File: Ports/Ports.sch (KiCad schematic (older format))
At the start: 22 parts, among them J1 Conn_01x09_Male, J2 Conn_01x09_Male, J3 Conn_01x09_Male, J4 Screw_Terminal_01x02, J5 Conn_01x03_Male, U1 74LS574, U2 74LS574

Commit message: Polishing Ports
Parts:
- C1: footprint Capacitor_THT:C_Disc_D5.1mm_W3.2mm_P5.00mm -> Capacitor_THT:C_Disc_D9.0mm_W5.0mm_P10.00mm
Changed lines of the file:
@@
 F 0 "C1" H 6615 5196 50  0000 L CNN
 F 1 "0.1uF" H 6615 5105 50  0000 L CNN
-F 2 "Capacitor_THT:C_Disc_D5.1mm_W3.2mm_P5.00mm" H 6538 5000 50  0001 C CNN
+F 2 "Capacitor_THT:C_Disc_D9.0mm_W5.0mm_P10.00mm" H 6538 5000 50  0001 C CNN
 F 3 "~" H 6500 5150 50  0001 C CNN
 	1    6500 5150

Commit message: Polishing Ports
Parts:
- removed J5: Conn_01x03_Male, Connector_PinHeader_2.54mm:PinHeader_1x03_P2.54mm_Vertical, symbol Connector:Conn_01x03_Male
- added D1, D10, D2, D3, D4, D5, D6, D7, D8, D9: LED, LED_THT:LED_Rectangular_W5.0mm_H2.0mm, symbol Device:LED
- added J5: Conn_01x04_Male, Connector_PinHeader_2.54mm:PinHeader_1x04_P2.54mm_Horizontal, symbol Connector:Conn_01x04_Male
- added R10, R11, R12, R13, R4, R5, R6, R7, R8, R9: 1k, Resistor_SMD:R_0805_2012Metric_Pad1.20x1.40mm_HandSolder, symbol Device:R
- J1: footprint Connector_PinHeader_2.54mm:PinHeader_1x09_P2.54mm_Vertical -> Connector_PinHeader_2.54mm:PinHeader_1x09_P2.54mm_Horizontal
- R1: footprint Resistor_THT:R_Axial_DIN0207_L6.3mm_D2.5mm_P10.16mm_Horizontal -> Resistor_THT:R_Axial_DIN0207_L6.3mm_D2.5mm_P15.24mm_Horizontal
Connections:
- net labels added: EN
- wire segments 47 -> 59
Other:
- moved on the sheet: R1, RV1

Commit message: Ports. Try to add buttons.
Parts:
- added D11, D12, D13, D14, D15, D16, D17, D18, D19, D20, D21, D22, D23, D24, D25, D26: 6x6-tact-btn, CommonLibrary:6x6-tact-btn, symbol CommonLibrary:6x6-tact-btn
- added D27, D28: LL4148, Diode_SMD:D_MiniMELF, symbol Diode:LL4148
- added J6: Conn_01x09_Male, Connector_PinHeader_2.54mm:PinHeader_1x09_P2.54mm_Horizontal, symbol Connector:Conn_01x09_Male
- added J7: Conn_01x02_Male, Connector_PinHeader_2.54mm:PinHeader_1x02_P2.54mm_Horizontal, symbol Connector:Conn_01x02_Male
- added R14, R15, R16, R17, R18, R19, R20, R21: 10k, Resistor_SMD:R_0805_2012Metric_Pad1.20x1.40mm_HandSolder, symbol Device:R
- added U3: 74LS574, Package_DIP:DIP-20_W7.62mm, symbol 74xx:74LS574
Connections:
- net GND: now also J6.9 (Pin_9), U3.10 (GND)
- net P0.6: now also D27.1 (K)
- net P0.7: now also D28.1 (K)
- net VCC: now also R14.2, R15.2, R16.2, R17.2, R18.2, R19.2, R20.2, R21.2, U3.20 (VCC)
- new net: D11.2, D13.2, D15.2, D17.2, D19.2, D21.2, D23.2, D25.2, D27.2 (A)
- new net: D12.2, D14.2, D16.2, D18.2, D20.2, D22.2, D24.2, D26.2, D28.2 (A)
- new net BUS0: J6.8 (Pin_8), U3.19 (Q0)
- new net BUS1: J6.7 (Pin_7), U3.18 (Q1)
- new net BUS2: J6.6 (Pin_6), U3.17 (Q2)
- new net BUS3: J6.5 (Pin_5), U3.16 (Q3)
- new net BUS4: J6.4 (Pin_4), U3.15 (Q4)
- new net BUS5: J6.3 (Pin_3), U3.14 (Q5)
- new net BUS6: J6.2 (Pin_2), U3.13 (Q6)
- new net BUS7: J6.1 (Pin_1), U3.12 (Q7)
- new net IN0.0: D11.1, D12.1, R14.1, U3.2 (D0)
- new net IN0.1: D13.1, D14.1, R15.1, U3.3 (D1)
- new net IN0.2: D15.1, D16.1, R16.1, U3.4 (D2)
- new net IN0.3: D17.1, D18.1, R17.1, U3.5 (D3)
- new net IN0.4: D19.1, D20.1, R18.1, U3.6 (D4)
- new net IN0.5: D21.1, D22.1, R19.1, U3.7 (D5)
- new net IN0.6: D23.1, D24.1, R20.1, U3.8 (D6)
- new net IN0.7: D25.1, D26.1, R21.1, U3.9 (D7)
- new net IN0.C: J7.1 (Pin_1), U3.11 (Cp)
- new net IN0.OE: J7.2 (Pin_2), U3.1 (OE)
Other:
- moved on the sheet: C1, C2, D1, D10, D2, D3, D4, D5, D6, D7, D8, D9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

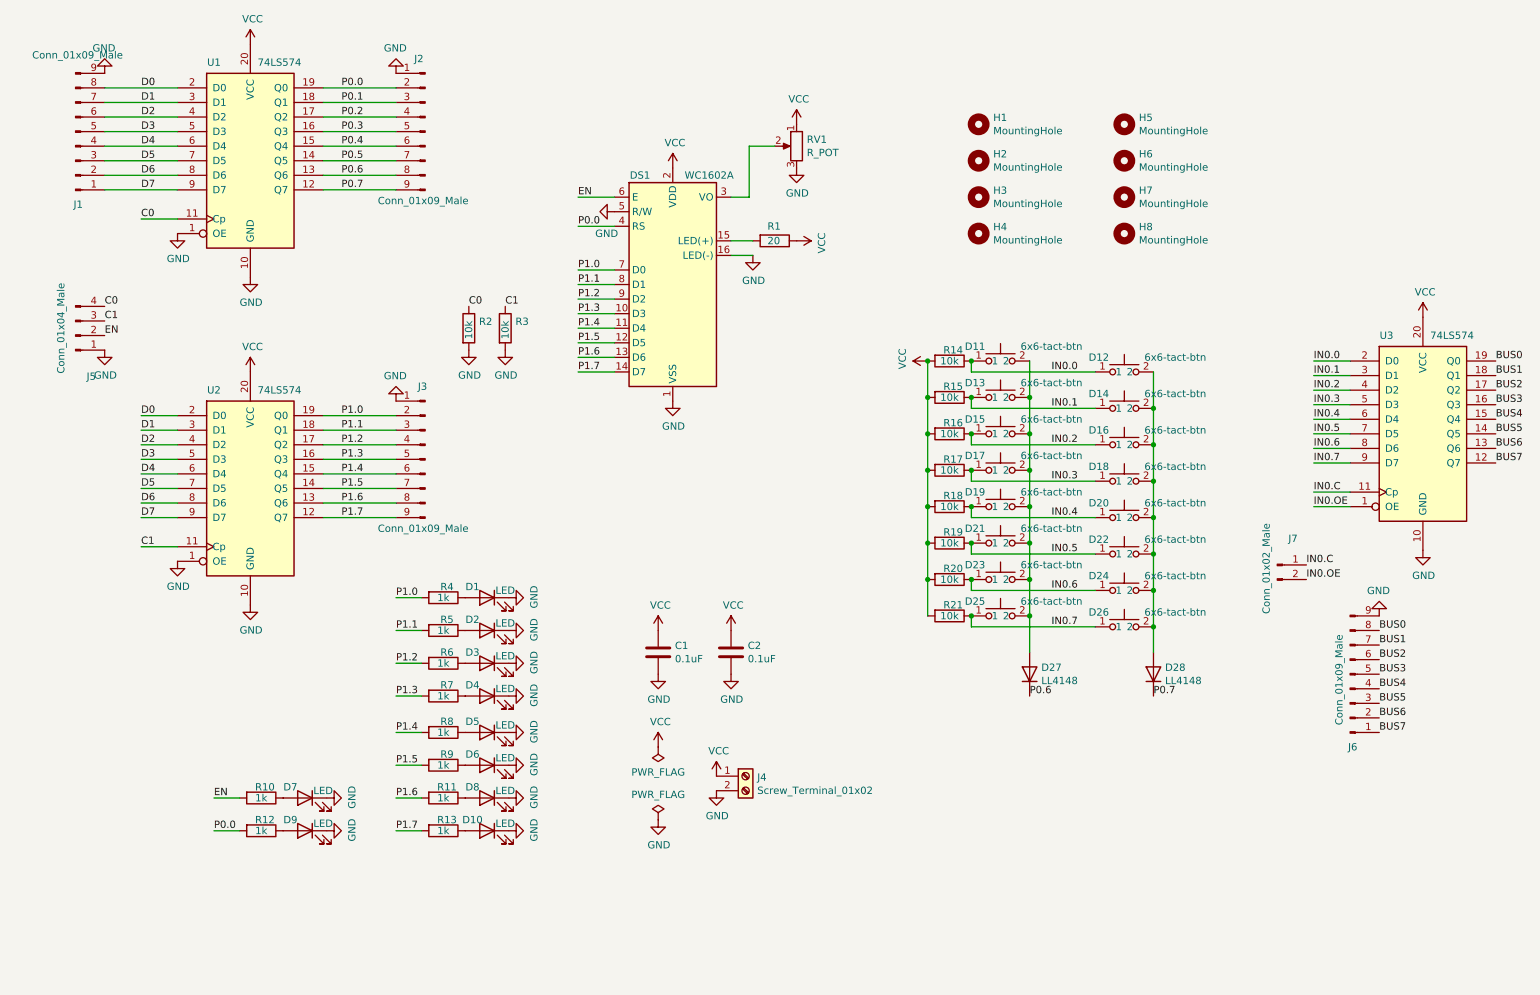
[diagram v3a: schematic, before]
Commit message: Add buttons to Ports&LCD pcb
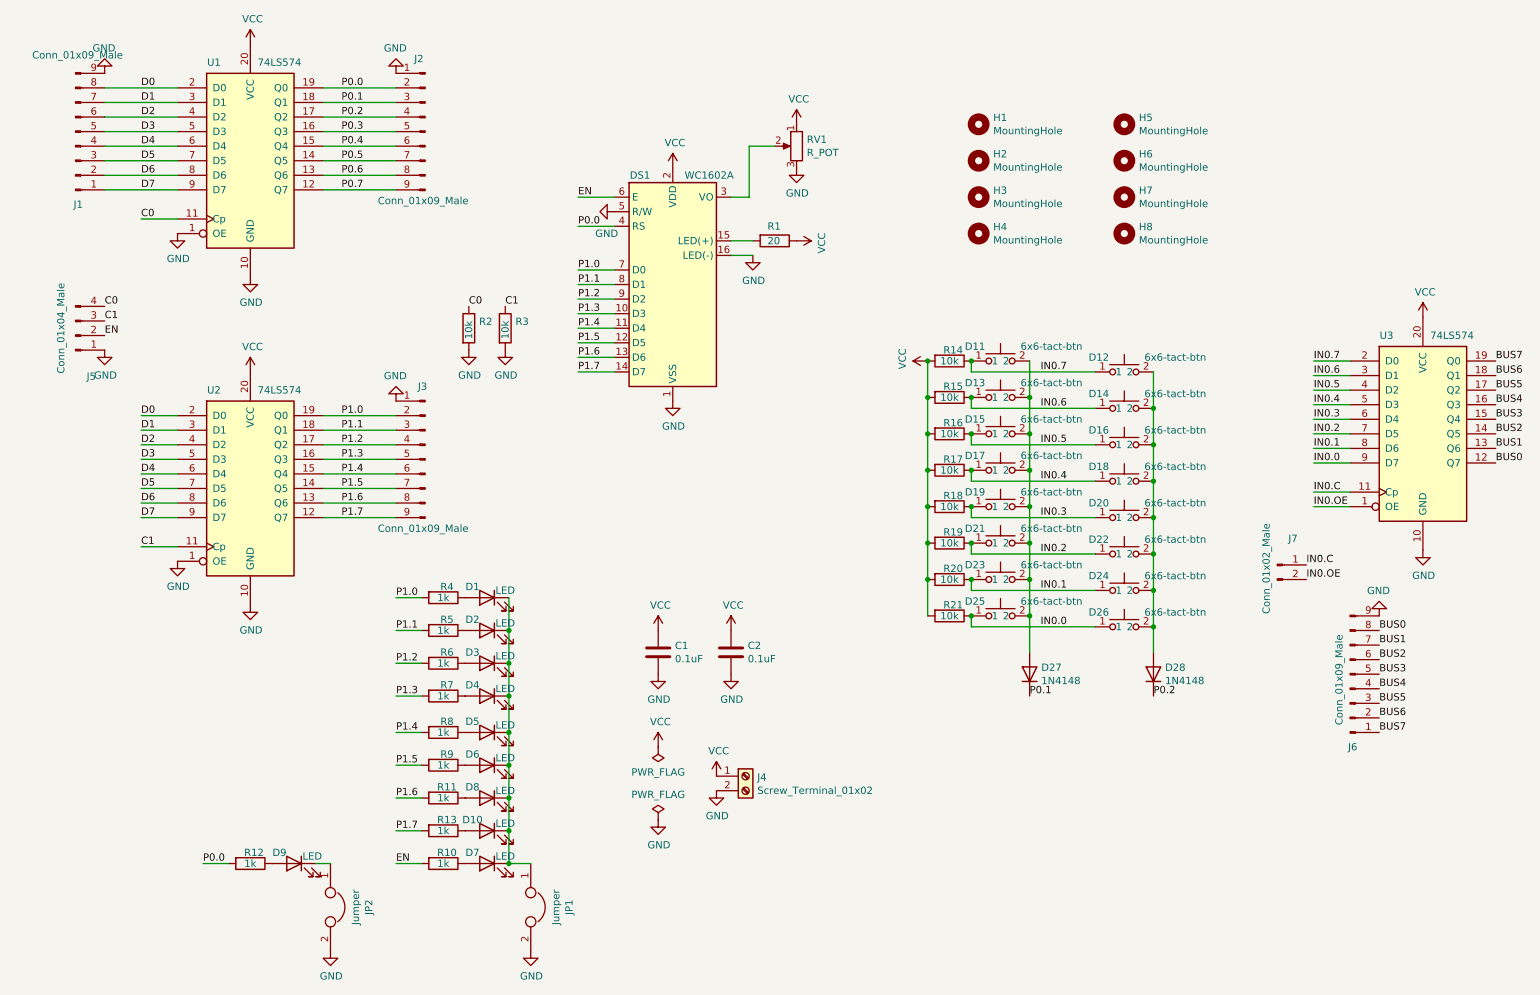
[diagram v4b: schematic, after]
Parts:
- removed D27, D28: LL4148, Diode_SMD:D_MiniMELF, symbol Diode:LL4148
- added D27, D28: 1N4148, Diode_THT:D_DO-15_P12.70mm_Horizontal, symbol Diode:1N4148
- added JP1, JP2: Jumper, Jumper:SolderJumper-2_P1.3mm_Open_RoundedPad1.0x1.5mm, symbol Device:Jumper
- D11, D12, D13, D14, D15, D16, D17, D18, D19, D20, D21, D22, D23, D24, D25, D26: footprint CommonLibrary:6x6-tact-btn -> Button_Switch_THT:SW_PUSH_6mm_H4.3mm
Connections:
- net BUS0: now also U3.12 (Q7); no longer U3.19 (Q0)
- net BUS1: now also U3.13 (Q6); no longer U3.18 (Q1)
- net BUS2: now also U3.14 (Q5); no longer U3.17 (Q2)
- net BUS3: now also U3.15 (Q4); no longer U3.16 (Q3)
- net BUS4: now also U3.16 (Q3); no longer U3.15 (Q4)
- net BUS5: now also U3.17 (Q2); no longer U3.14 (Q5)
- net BUS6: now also U3.18 (Q1); no longer U3.13 (Q6)
- net BUS7: now also U3.19 (Q0); no longer U3.12 (Q7)
- net GND: now also JP1.2, JP2.2; no longer D1.1 (K), D10.1 (K), D2.1 (K), D3.1 (K), D4.1 (K), D5.1 (K), D6.1 (K), D7.1 (K), D8.1 (K), D9.1 (K)
- net IN0.0: now also D25.1, D26.1, R21.1, U3.9 (D7); no longer D11.1, D12.1, R14.1, U3.2 (D0)
- net IN0.1: now also D23.1, D24.1, R20.1, U3.8 (D6); no longer D13.1, D14.1, R15.1, U3.3 (D1)
- net IN0.2: now also D21.1, D22.1, R19.1, U3.7 (D5); no longer D15.1, D16.1, R16.1, U3.4 (D2)
- net IN0.3: now also D19.1, D20.1, R18.1, U3.6 (D4); no longer D17.1, D18.1, R17.1, U3.5 (D3)
- net IN0.4: now also D17.1, D18.1, R17.1, U3.5 (D3); no longer D19.1, D20.1, R18.1, U3.6 (D4)
- net IN0.5: now also D15.1, D16.1, R16.1, U3.4 (D2); no longer D21.1, D22.1, R19.1, U3.7 (D5)
- net IN0.6: now also D13.1, D14.1, R15.1, U3.3 (D1); no longer D23.1, D24.1, R20.1, U3.8 (D6)
- net IN0.7: now also D11.1, D12.1, R14.1, U3.2 (D0); no longer D25.1, D26.1, R21.1, U3.9 (D7)
- net P0.1: now also D27.1 (K)
- net P0.2: now also D28.1 (K)
- net at D11.2, D13.2, D15.2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: now also D27.2 (A)
- net at D12.2, D14.2, D16.2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: now also D28.2 (A)
- new net: D1.1 (K), D10.1 (K), D2.1 (K), D3.1 (K), D4.1 (K), D5.1 (K), D6.1 (K), D7.1 (K), D8.1 (K), JP1.1
- new net: D9.1 (K), JP2.1
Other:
- moved on the sheet: D7, D9, R10, R12

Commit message: Polishing Ports & LCD
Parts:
- added C3, C4: 0.1uF, Capacitor_SMD:C_1206_3216Metric_Pad1.42x1.75mm_HandSolder, symbol Device:C
- C1: footprint Capacitor_THT:C_Disc_D9.0mm_W5.0mm_P10.00mm -> Capacitor_SMD:C_1206_3216Metric_Pad1.42x1.75mm_HandSolder
- C2: footprint Capacitor_THT:C_Disc_D5.1mm_W3.2mm_P5.00mm -> Capacitor_SMD:C_1206_3216Metric_Pad1.42x1.75mm_HandSolder
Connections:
- net GND: now also RV1.1, C3.2, C4.2; no longer RV1.3
- net VCC: now also RV1.3, C3.1, C4.1; no longer RV1.1
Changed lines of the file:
@@
 F 3 "~" H 5950 1775 50  0001 C CNN
 	1    5950 1775
-	-1   0    0    -1
+	-1   0    0    1
 $EndComp
 $Comp
@@
 F 0 "C1" H 5115 5296 50  0000 L CNN
 F 1 "0.1uF" H 5115 5205 50  0000 L CNN
-F 2 "Capacitor_THT:C_Disc_D9.0mm_W5.0mm_P10.00mm" H 5038 5100 50  0001 C CNN
+F 2 "Capacitor_SMD:C_1206_3216Metric_Pad1.42x1.75mm_HandSolder" H 5038 5100 50  0001 C CNN
 F 3 "~" H 5000 5250 50  0001 C CNN
 	1    5000 5250
@@
 F 0 "C2" H 5615 5296 50  0000 L CNN
 F 1 "0.1uF" H 5615 5205 50  0000 L CNN
-F 2 "Capacitor_THT:C_Disc_D5.1mm_W3.2mm_P5.00mm" H 5538 5100 50  0001 C CNN
+F 2 "Capacitor_SMD:C_1206_3216Metric_Pad1.42x1.75mm_HandSolder" H 5538 5100 50  0001 C CNN
 F 3 "~" H 5500 5250 50  0001 C CNN
 	1    5500 5250
@@
 	0    1    1    0
 $EndComp
+$Comp
+L Device:C C3
+U 1 1 64B8A916
+P 6000 5250
+F 0 "C3" H 6115 5296 50  0000 L CNN
+F 1 "0.1uF" H 6115 5205 50  0000 L CNN
+F 2 "Capacitor_SMD:C_1206_3216Metric_Pad1.42x1.75mm_HandSolder" H 6038 5100 50  0001 C CNN
+F 3 "~" H 6000 5250 50  0001 C CNN
+	1    6000 5250
+	1    0    0    -1
+$EndComp
+$Comp
+L power:VCC #PWR017
+U 1 1 64B8A91C
+P 6000 5100
+F 0 "#PWR017" H 6000 4950 50  0001 C CNN
+F 1 "VCC" H 6015 5273 50  0000 C CNN
+F 2 "" H 6000 5100 50  0001 C CNN
+F 3 "" H 6000 5100 50  0001 C CNN
+	1    6000 5100
+	1    0    0    -1
+$EndComp
+$Comp
+L power:GND #PWR018
+U 1 1 64B8A922
+P 6000 5400
+F 0 "#PWR018" H 6000 5150 50  0001 C CNN
+F 1 "GND" H 6005 5227 50  0000 C CNN
+F 2 "" H 6000 5400 50  0001 C CNN
+F 3 "" H 6000 5400 50  0001 C CNN
+	1    6000 5400
+	1    0    0    -1
+$EndComp
+$Comp
+L Device:C C4
+U 1 1 64BCC7FB
+P 6500 5250
+F 0 "C4" H 6615 5296 50  0000 L CNN
+F 1 "0.1uF" H 6615 5205 50  0000 L CNN
+F 2 "Capacitor_SMD:C_1206_3216Metric_Pad1.42x1.75mm_HandSolder" H 6538 5100 50  0001 C CNN
+F 3 "~" H 6500 5250 50  0001 C CNN
+	1    6500 5250
+	1    0    0    -1
+$EndComp
+$Comp
+L power:VCC #PWR0118
+U 1 1 64BCC801
+P 6500 5100
+F 0 "#PWR0118" H 6500 4950 50  0001 C CNN
+F 1 "VCC" H 6515 5273 50  0000 C CNN
+F 2 "" H 6500 5100 50  0001 C CNN
+F 3 "" H 6500 5100 50  0001 C CNN
+	1    6500 5100
+	1    0    0    -1
+$EndComp
+$Comp
+L power:GND #PWR0119
+U 1 1 64BCC807
+P 6500 5400
+F 0 "#PWR0119" H 6500 5150 50  0001 C CNN
+F 1 "GND" H 6505 5227 50  0000 C CNN
+F 2 "" H 6500 5400 50  0001 C CNN
+F 3 "" H 6500 5400 50  0001 C CNN
+	1    6500 5400
+	1    0    0    -1
+$EndComp
 $EndSCHEMATC

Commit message: Polishing Ports
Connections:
- net C0 renamed OUT0
- net C1 renamed OUT1
- net EN renamed C2
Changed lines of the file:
@@
 D7
 Text Label 1450 4525 0    50   ~ 0
-C1
+OUT1
 $Comp
 L power:GND #PWR08
@@
 $EndComp
 Text Label 1450 2275 0    50   ~ 0
-C0
+OUT0
 $Comp
 L power:GND #PWR02
@@
 $EndComp
 Text Label 1200 2875 0    50   ~ 0
-C0
+OUT0
 Text Label 1200 2975 0    50   ~ 0
-C1
+OUT1
 Wire Wire Line
 	1450 2275 1700 2275
@@
 $EndComp
 Text Label 3700 2875 0    50   ~ 0
-C0
+OUT0
 Text Label 3950 2875 0    50   ~ 0
-C1
+OUT1
 $Comp
 L Connector:Conn_01x04_Male J5
@@
 $EndComp
 Text Label 1200 3075 0    50   ~ 0
-EN
+C2
 Text Label 4450 2125 0    50   ~ 0
-EN
+C2
 $Comp
 L Device:LED D1
@@
 P1.7
 Text Label 3200 6700 0    50   ~ 0
-EN
+C2
 Text Label 1875 6700 0    50   ~ 0
 P0.0

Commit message: Polishing Ports
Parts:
- added J8: Conn_01x08_Male, Connector_PinHeader_2.54mm:PinHeader_1x08_P2.54mm_Vertical, symbol Connector:Conn_01x08_Male
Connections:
- net IN0.0: now also J8.8 (Pin_8)
- net IN0.1: now also J8.7 (Pin_7)
- net IN0.2: now also J8.6 (Pin_6)
- net IN0.3: now also J8.5 (Pin_5)
- net IN0.4: now also J8.4 (Pin_4)
- net IN0.5: now also J8.3 (Pin_3)
- net IN0.6: now also J8.2 (Pin_2)
- net IN0.7: now also J8.1 (Pin_1)
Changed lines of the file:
@@
+	1    0    0    -1
+$EndComp
+$Comp
+L Connector:Conn_01x08_Male J8
+U 1 1 64B9E326
+P 9300 3550
+F 0 "J8" H 9408 4031 50  0000 C CNN
+F 1 "Conn_01x08_Male" V 9250 3525 50  0000 C CNN
+F 2 "Connector_PinHeader_2.54mm:PinHeader_1x08_P2.54mm_Vertical" H 9300 3550 50  0001 C CNN
+F 3 "~" H 9300 3550 50  0001 C CNN
+	1    9300 3550
 	1    0    0    -1
 $EndComp

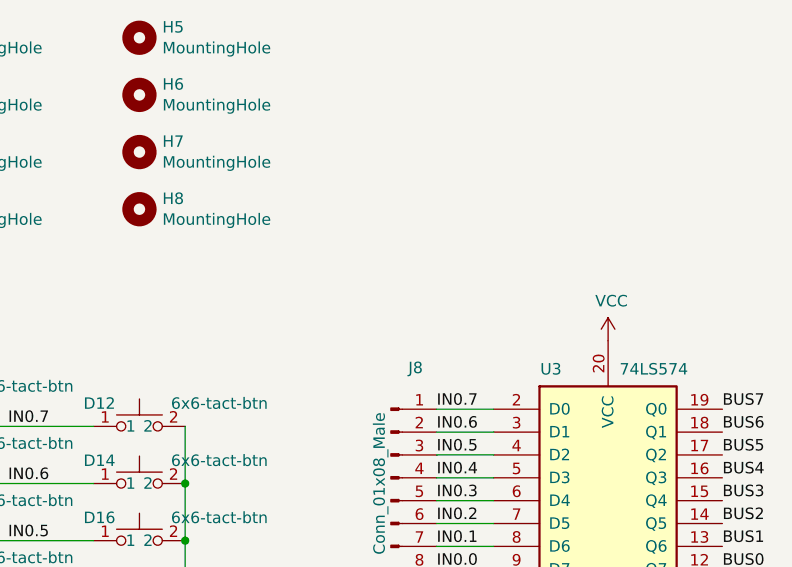
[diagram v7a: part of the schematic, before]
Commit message: Ports. Add more gnd pins
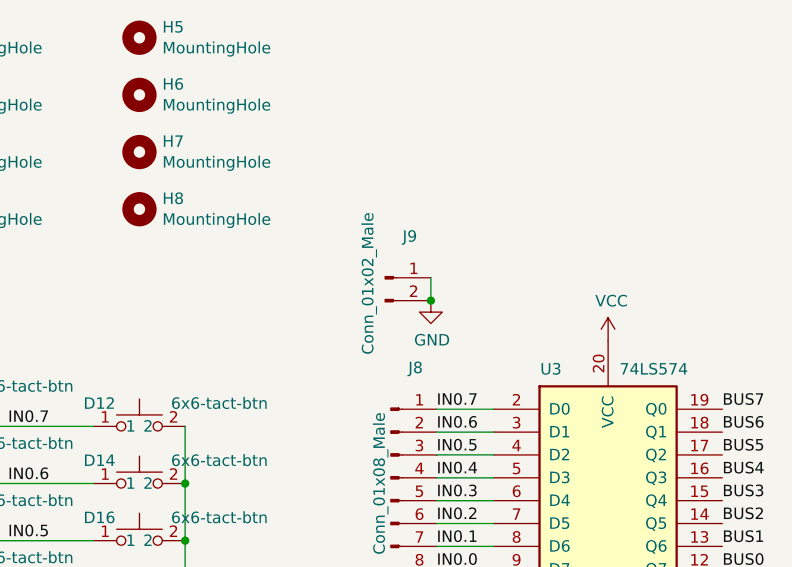
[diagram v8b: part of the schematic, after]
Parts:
- added J9: Conn_01x02_Male, Connector_PinHeader_2.54mm:PinHeader_1x02_P2.54mm_Vertical, symbol Connector:Conn_01x02_Male
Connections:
- net GND: now also J9.1 (Pin_1), J9.2 (Pin_2)
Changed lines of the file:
@@
 	1    0    0    -1
 $EndComp
+$Comp
+L Connector:Conn_01x02_Male J9
+U 1 1 64BB2BFF
+P 9275 2675
+F 0 "J9" H 9383 2856 50  0000 C CNN
+F 1 "Conn_01x02_Male" V 9200 2650 50  0000 C CNN
+F 2 "Connector_PinHeader_2.54mm:PinHeader_1x02_P2.54mm_Vertical" H 9275 2675 50  0001 C CNN
+F 3 "~" H 9275 2675 50  0001 C CNN
+	1    9275 2675
+	1    0    0    -1
+$EndComp
+$Comp
+L power:GND #PWR019
+U 1 1 64BB6028
+P 9475 2775
+F 0 "#PWR019" H 9475 2525 50  0001 C CNN
+F 1 "GND" H 9480 2602 50  0000 C CNN
+F 2 "" H 9475 2775 50  0001 C CNN
+F 3 "" H 9475 2775 50  0001 C CNN
+	1    9475 2775
+	1    0    0    -1
+$EndComp
+Wire Wire Line
+	9475 2675 9475 2775
+Connection ~ 9475 2775
 $EndSCHEMATC
